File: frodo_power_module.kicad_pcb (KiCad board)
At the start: 2 copper layers, 91.1 x 72.6 mm, 76 parts, among them J1 Keystone 1048, J10 SWD Header, J2 Molex MicroFit 2x3, J3 Molex MicroFit 2x2, J4 Molex MicroFit 2x2, J5 JST-GH, J6 JST-GH, J7 Molex MicroFit 2x3, U1 STM32F042F6Px, U2 L7805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

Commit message: changed zones
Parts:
- moved J6 5.03 mm to (141.0, 48.7)
- moved J5 4.95 mm to (122.6, 48.8)
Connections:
- net Net-(J2-Pin_3) renamed /Net-
- net Net-(J2-Pin_6) renamed /Net+
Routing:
- net CAN+: track 94.5 -> 99.8 mm
- net CAN-: track 94.6 -> 99.8 mm
- net /Net+: track 42.5 -> 44.6 mm
- net /Net-: track 42.4 -> 43.9 mm

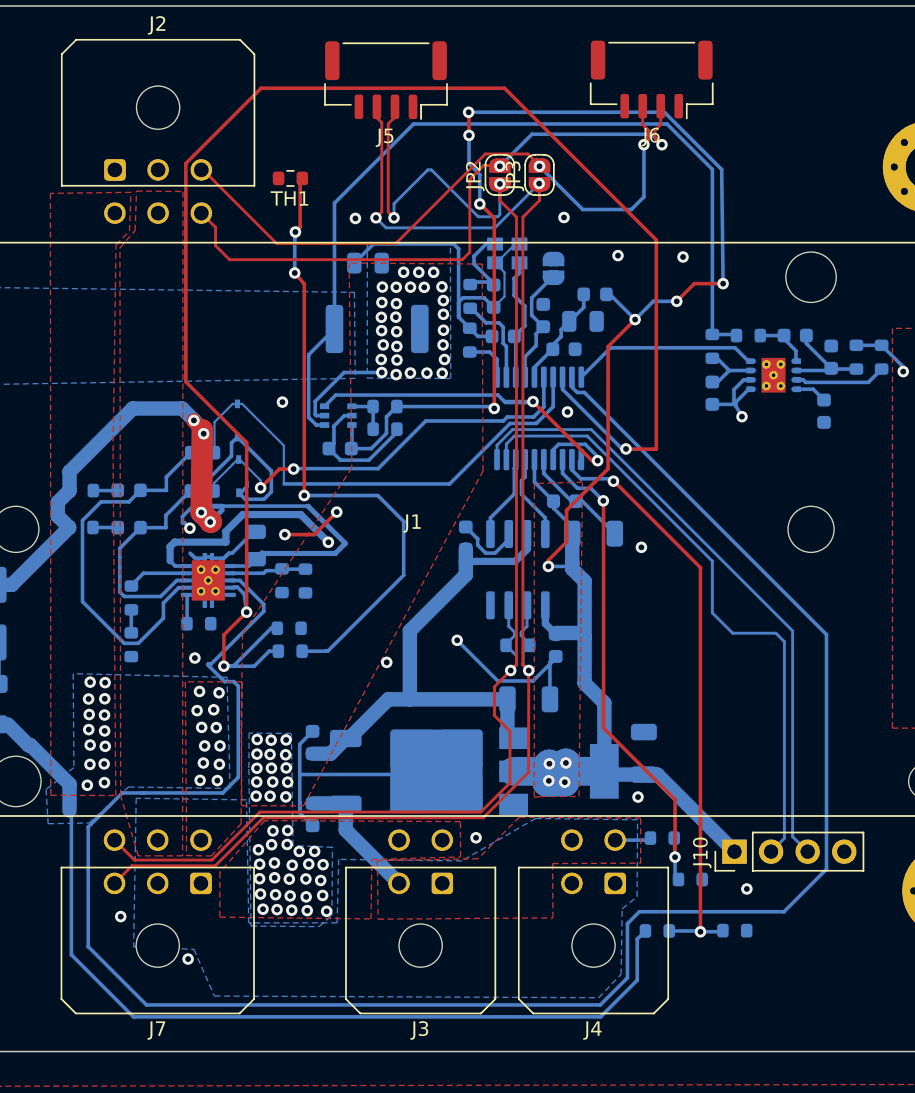
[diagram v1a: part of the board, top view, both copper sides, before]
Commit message: Minor trace tweaks
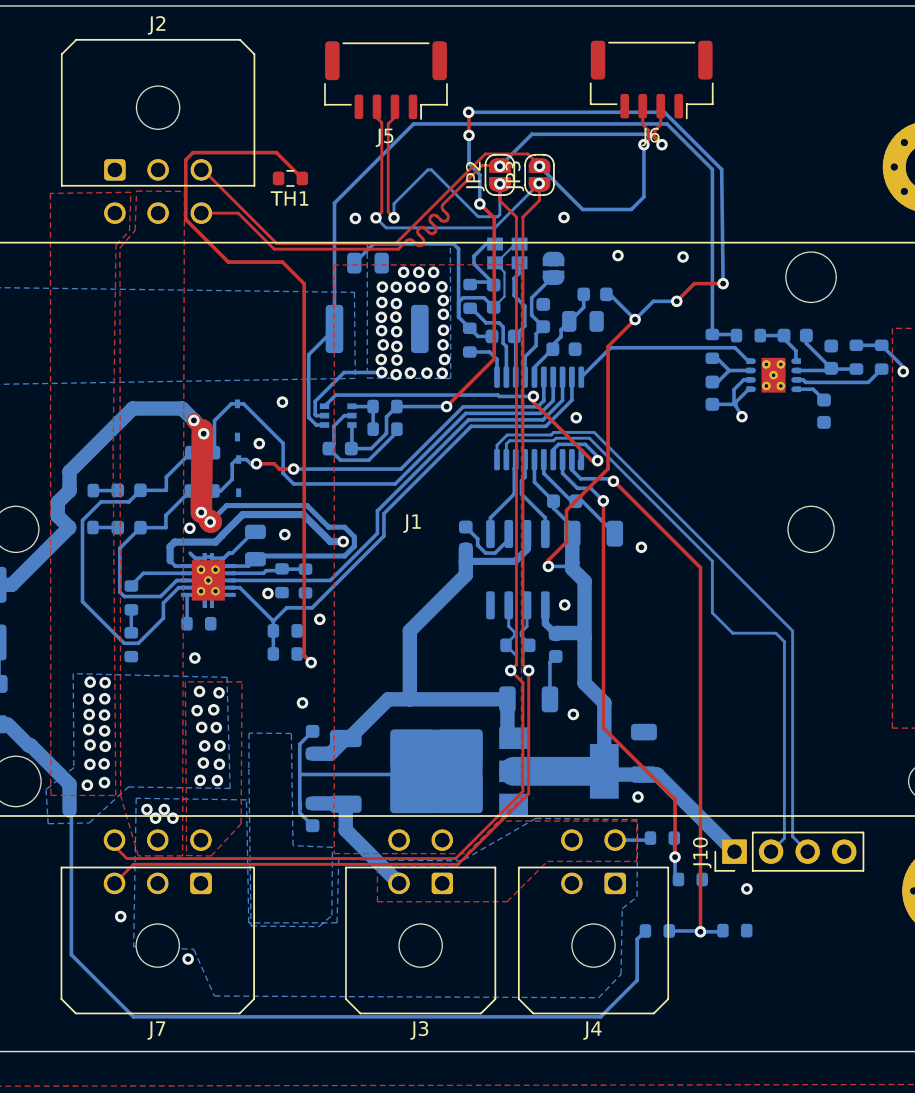
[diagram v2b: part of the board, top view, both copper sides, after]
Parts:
- moved R10 0.40 mm to (115.6, 88.6)
- moved R9 0.33 mm to (115.6, 87.0)
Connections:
- U1 pad 8: NTC -> CHARGE_ENABLE
- U1 pad 9: CHARGE_ENABLE -> NTC
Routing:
- net CHARGE_ENABLE: track 139.1 -> 30.8 mm
- net NTC: track 111.6 -> 35.9 mm, vias 3 -> 0
- net GND: track 113.4 -> 83.6 mm, vias 20 -> 22
- net +3V3: track 145.6 -> 137.4 mm, vias 12 -> 8
- net Net-(R10-Pad2): track 43.7 -> 51.2 mm, vias 3 -> 1
- net ISENSE: track 27.7 -> 25.9 mm
- net STAT2: track 30.2 -> 28.5 mm
- net CAN-: track 99.8 -> 100.7 mm
- net CAN+: track 99.8 -> 100.7 mm
- net STAT1: track 34.5 -> 33.8 mm
- net +BATT: track 22.2 -> 22.8 mm, vias 71 -> 29
- net +VSW: vias 0 -> 4
- removed copper zone on F.Cu, net +3V3

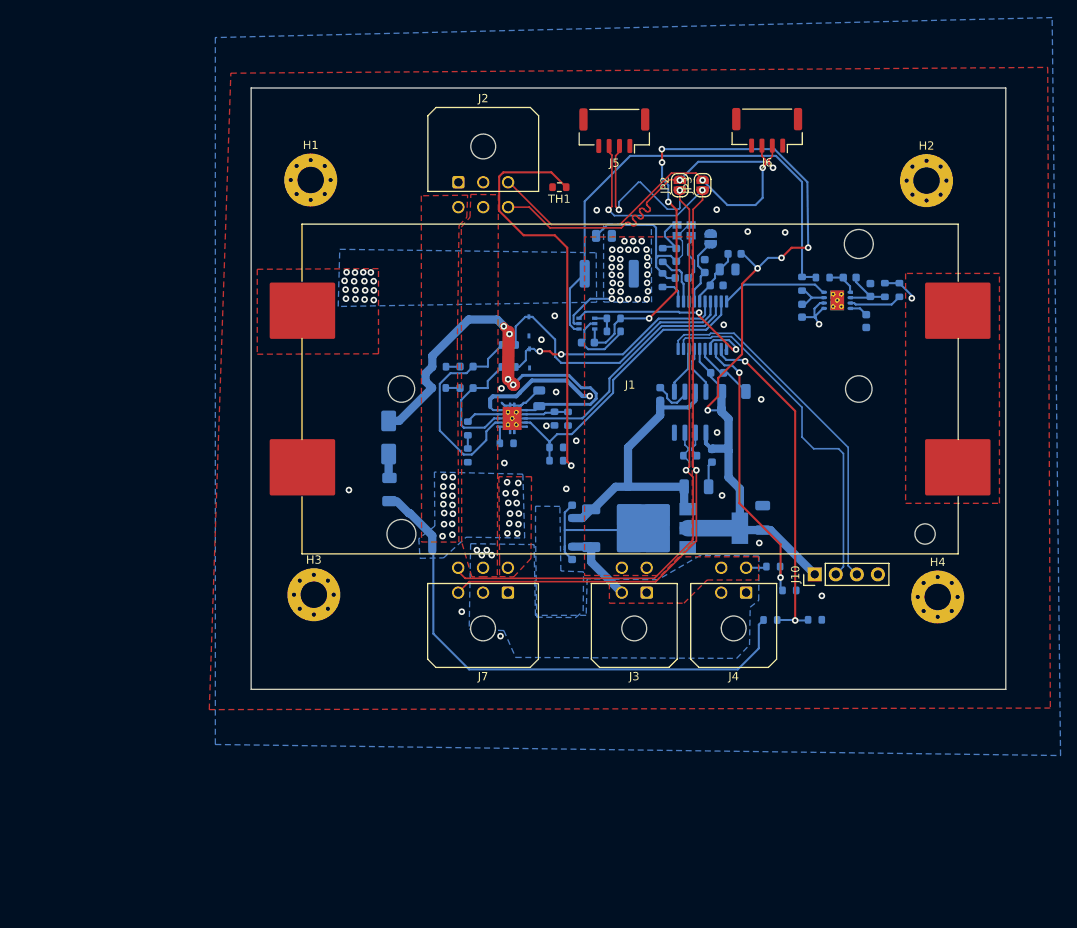
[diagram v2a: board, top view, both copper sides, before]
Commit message: clear DRC msgs, align elements to grid
After updating the design constraints according to the JLCPCB manufacturing capabilities, the PTHs
of component U5 were to small (0.25mm diameter, min. is 0.3mm). Note that after resolving this error,
the DRC now shows a warning about a modified footprint of U5.
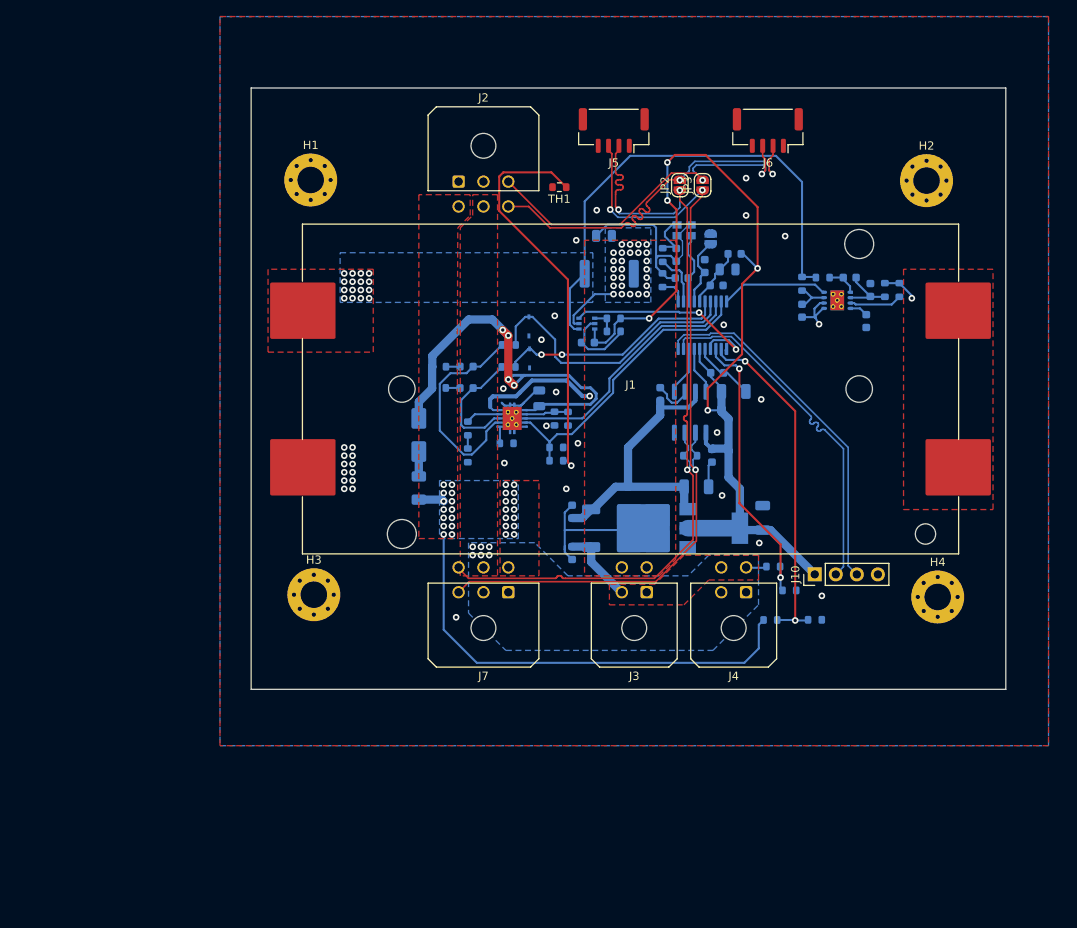
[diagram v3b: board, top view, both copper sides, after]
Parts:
- moved D1 3.66 mm to (99.0, 85.5)
- moved F1 3.55 mm to (99.0, 91.9)
- moved J6 0.09 mm to (141.1, 48.8)
- moved J2 0.08 mm to (103.8, 54.9)
- moved J5 0.07 mm to (122.5, 48.8)
- moved J7 0.07 mm to (109.8, 104.5)
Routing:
- net +3V3: track 137.4 -> 122.1 mm, vias 8 -> 5
- net VDC: track 64.6 -> 58.7 mm, vias 26 -> 28
- net Net-(R10-Pad2): track 51.2 -> 49.0 mm
- net Net-(D1-K): track 52.0 -> 50.3 mm
- net /Net+: track 44.5 -> 45.6 mm
- net VSENSE_BATT: track 34.5 -> 35.1 mm
- net Net-(D2-K): track 26.0 -> 25.5 mm
- net Net-(D3-K): track 15.3 -> 14.8 mm
- net +BATT: track 22.8 -> 23.2 mm, vias 29 -> 27
- net GND: vias 22 -> 33
- net +VSW: vias 4 -> 6

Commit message: Replace parts with JLCPCB basic ones where possible, replace crystal footprint
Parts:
- Y1: footprint Oscillator:Oscillator_SMD_SeikoEpson_SG210-4Pin_2.5x2.0mm -> Crystal:Crystal_SMD_5032-4Pin_5.0x3.2mm
- moved JP1 2.24 mm to (136.3, 61.0)
- moved Y1 1.29 mm to (132.2, 60.3)
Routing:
- net NRST: track 8.45 -> 11.0 mm
- net GND: track 83.6 -> 81.9 mm

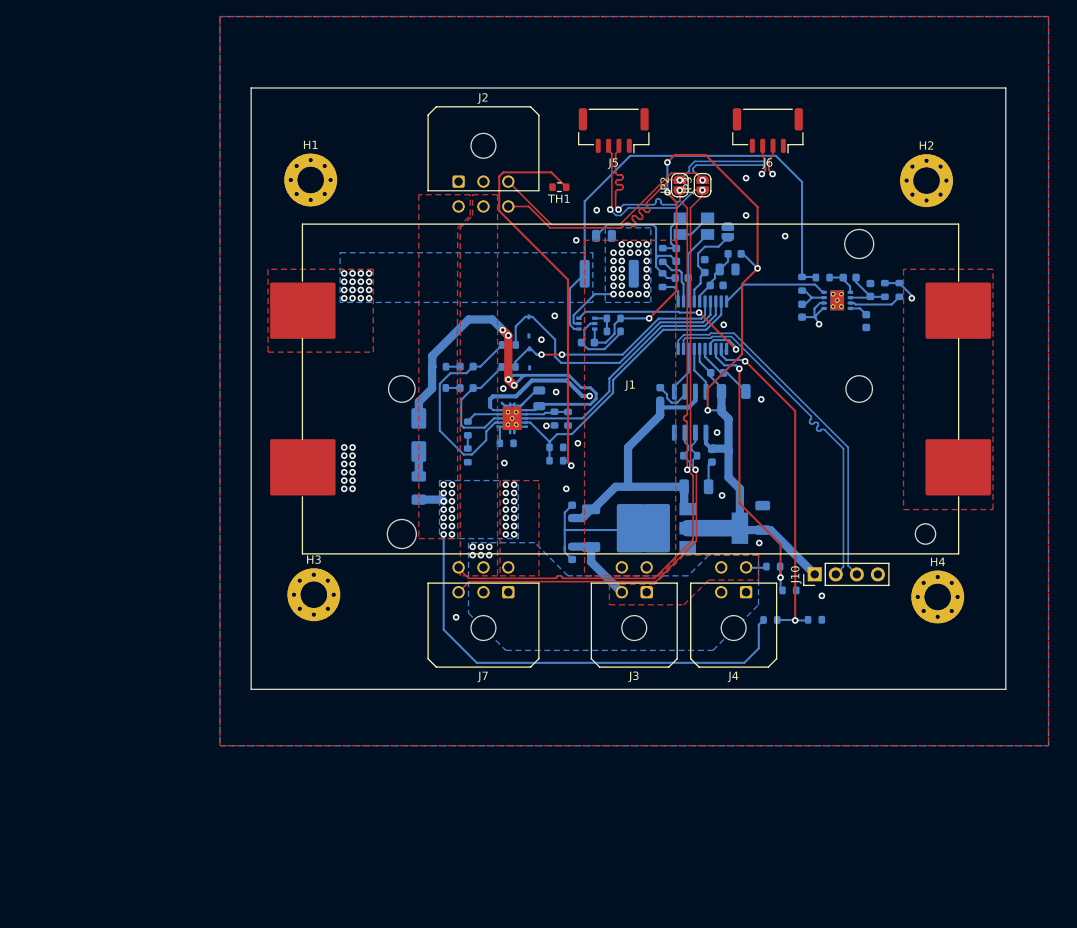
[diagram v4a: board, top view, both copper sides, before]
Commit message: Minor routing changes, add outline
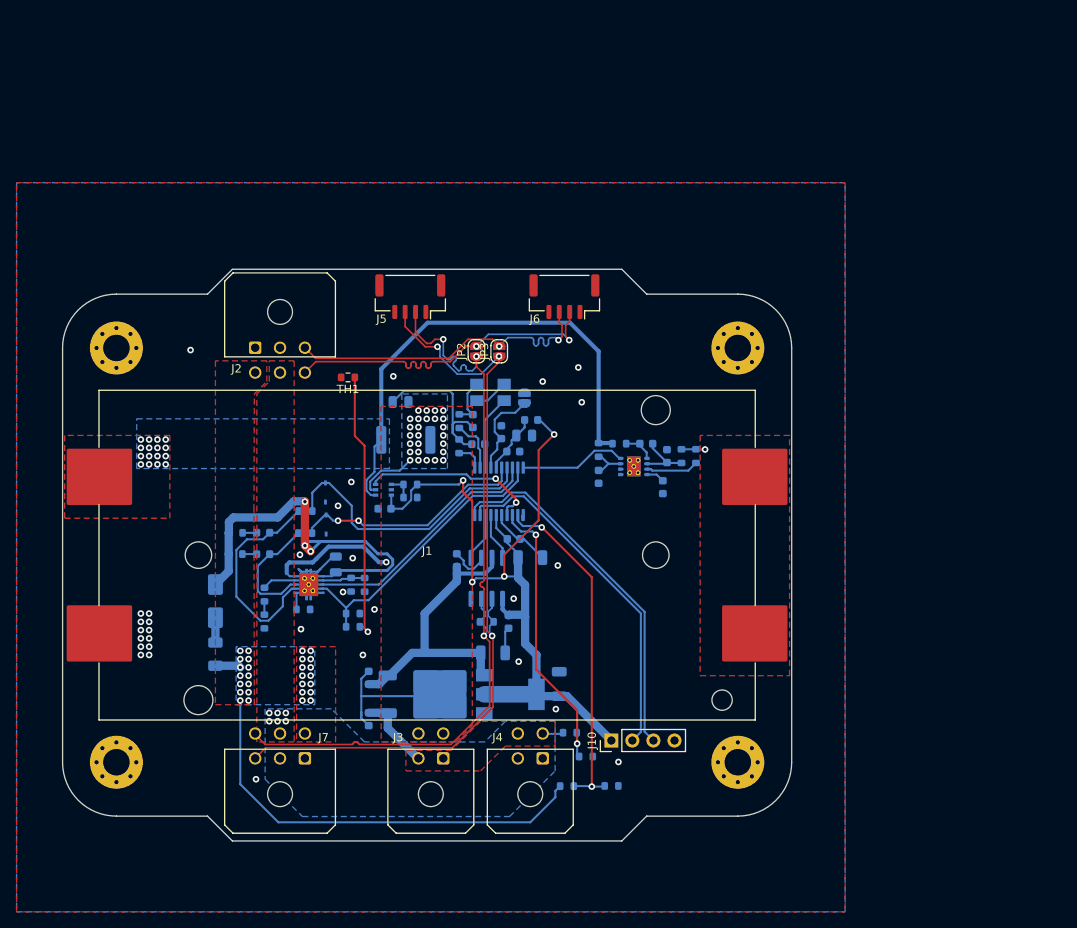
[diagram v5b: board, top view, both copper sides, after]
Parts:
- moved TH1 34.3 mm to (90.5, 78.5)
- moved U7 31.7 mm to (94.7, 92.1)
- moved C16 31.7 mm to (128.9, 88.0)
- moved C17 31.7 mm to (128.4, 91.8)
- moved C7 31.7 mm to (111.7, 85.6)
- moved D2 31.7 mm to (80.2, 97.3)
- moved D3 31.7 mm to (80.2, 99.9)
- moved D6 31.7 mm to (87.8, 96.3)
- moved J5 31.7 mm to (98.0, 68.8)
- moved JP1 31.7 mm to (111.8, 81.0)
- moved R16 31.7 mm to (130.7, 88.0)
- moved R17 31.7 mm to (132.4, 88.0)
- moved R18 31.7 mm to (98.0, 91.5)
- moved R19 31.7 mm to (98.0, 93.0)
- moved R21 31.7 mm to (122.3, 127.9)
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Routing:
- net +3V3: track 122.1 -> 99.2 mm, vias 5 -> 4
- net Net-(R10-Pad2): track 49.0 -> 32.6 mm
- net GND: track 81.9 -> 65.9 mm, vias 33 -> 31
- net /Net-: track 44.1 -> 39.5 mm
- net /Net+: track 45.6 -> 41.1 mm
- net ISENSE: track 25.7 -> 21.6 mm
- net CAN-: track 100.4 -> 96.7 mm
- net CAN+: track 100.3 -> 96.6 mm
- net VDC: track 58.7 -> 56.0 mm
- net Net-(D1-K): track 50.3 -> 47.7 mm, vias 4 -> 3
- net Net-(J1-Pin_2): track 4.20 -> 2.86 mm
- net CHARGE_ENABLE: track 30.8 -> 29.9 mm
- net NTC: track 35.9 -> 35.0 mm
- net SWCLK: track 43.4 -> 44.1 mm
- net SWDIO: track 43.3 -> 42.5 mm
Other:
- board size 91.1 x 72.6 mm -> 88 x 69 mm

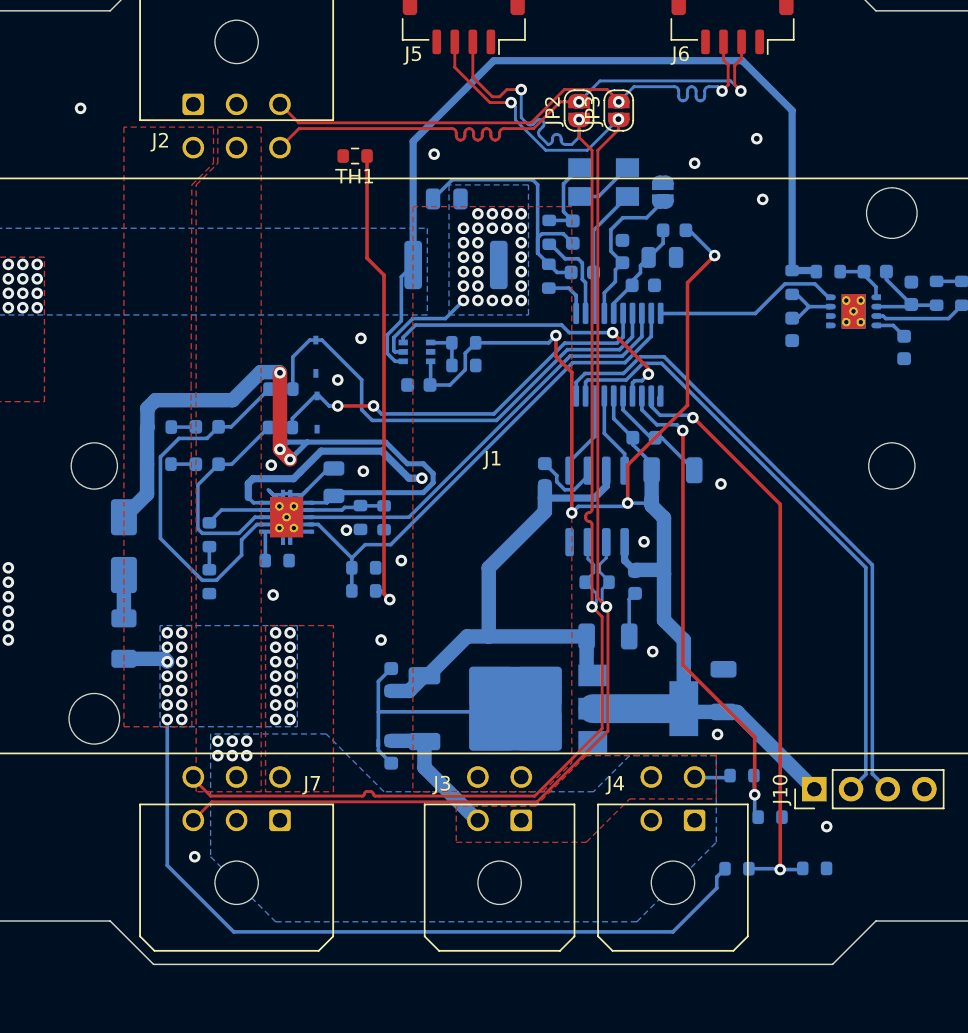
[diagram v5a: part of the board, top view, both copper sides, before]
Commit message: added capacitors. By updating pcb the old Osci footprint was restored. This needs to be changed
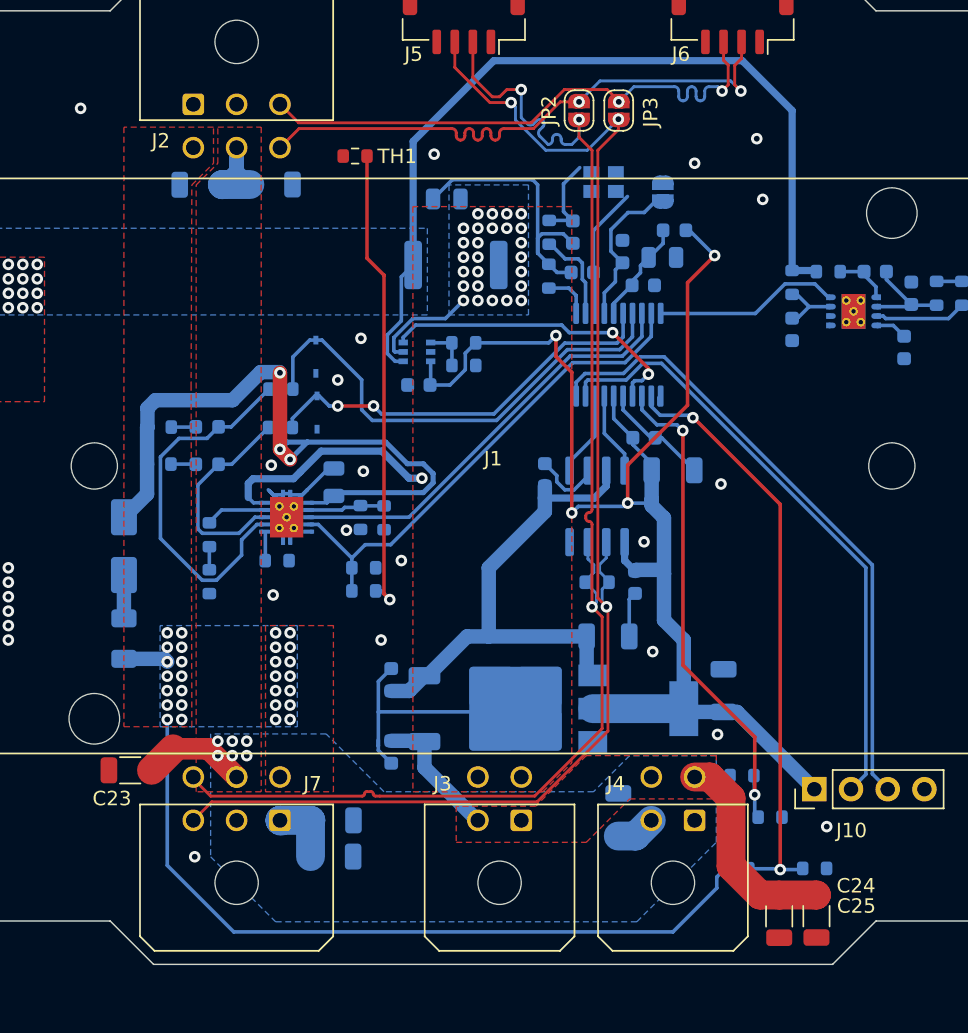
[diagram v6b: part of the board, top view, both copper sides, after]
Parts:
- added C21: 47u, Capacitor_SMD:C_1206_3216Metric, B.Cu at (88.8, 127.0)
- added C22: 47u, Capacitor_SMD:C_1206_3216Metric, B.Cu at (88.9, 124.5)
- added C23: 47u, Capacitor_SMD:C_1206_3216Metric, F.Cu at (74.9, 121.1)
- added C24: 47u, Capacitor_SMD:C_1206_3216Metric, F.Cu at (119.8, 131.2)
- added C25: 47u, Capacitor_SMD:C_1206_3216Metric, F.Cu at (122.4, 131.2)
- added C26: 47u, Capacitor_SMD:C_1206_3216Metric, B.Cu at (108.7, 124.1)
- added C27: 47u, Capacitor_SMD:C_1206_3216Metric, B.Cu at (79.8, 80.5)
- added C28: 47u, Capacitor_SMD:C_1206_3216Metric, B.Cu at (84.6, 80.5)
- D2: value green -> yellow
- JP1, JP2, JP3: value SolderJumper_2_Open -> r
- Y1: footprint Crystal:Crystal_SMD_5032-4Pin_5.0x3.2mm -> Oscillator:Oscillator_SMD_SeikoEpson_SG210-4Pin_2.5x2.0mm
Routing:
- net +VSW: track 11.9 -> 41.6 mm
- net GND: track 65.9 -> 69.3 mm
